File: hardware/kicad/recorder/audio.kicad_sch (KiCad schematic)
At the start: 20 parts, among them U2 ES8311, U6 NS4150B, Y1 12.288MHz

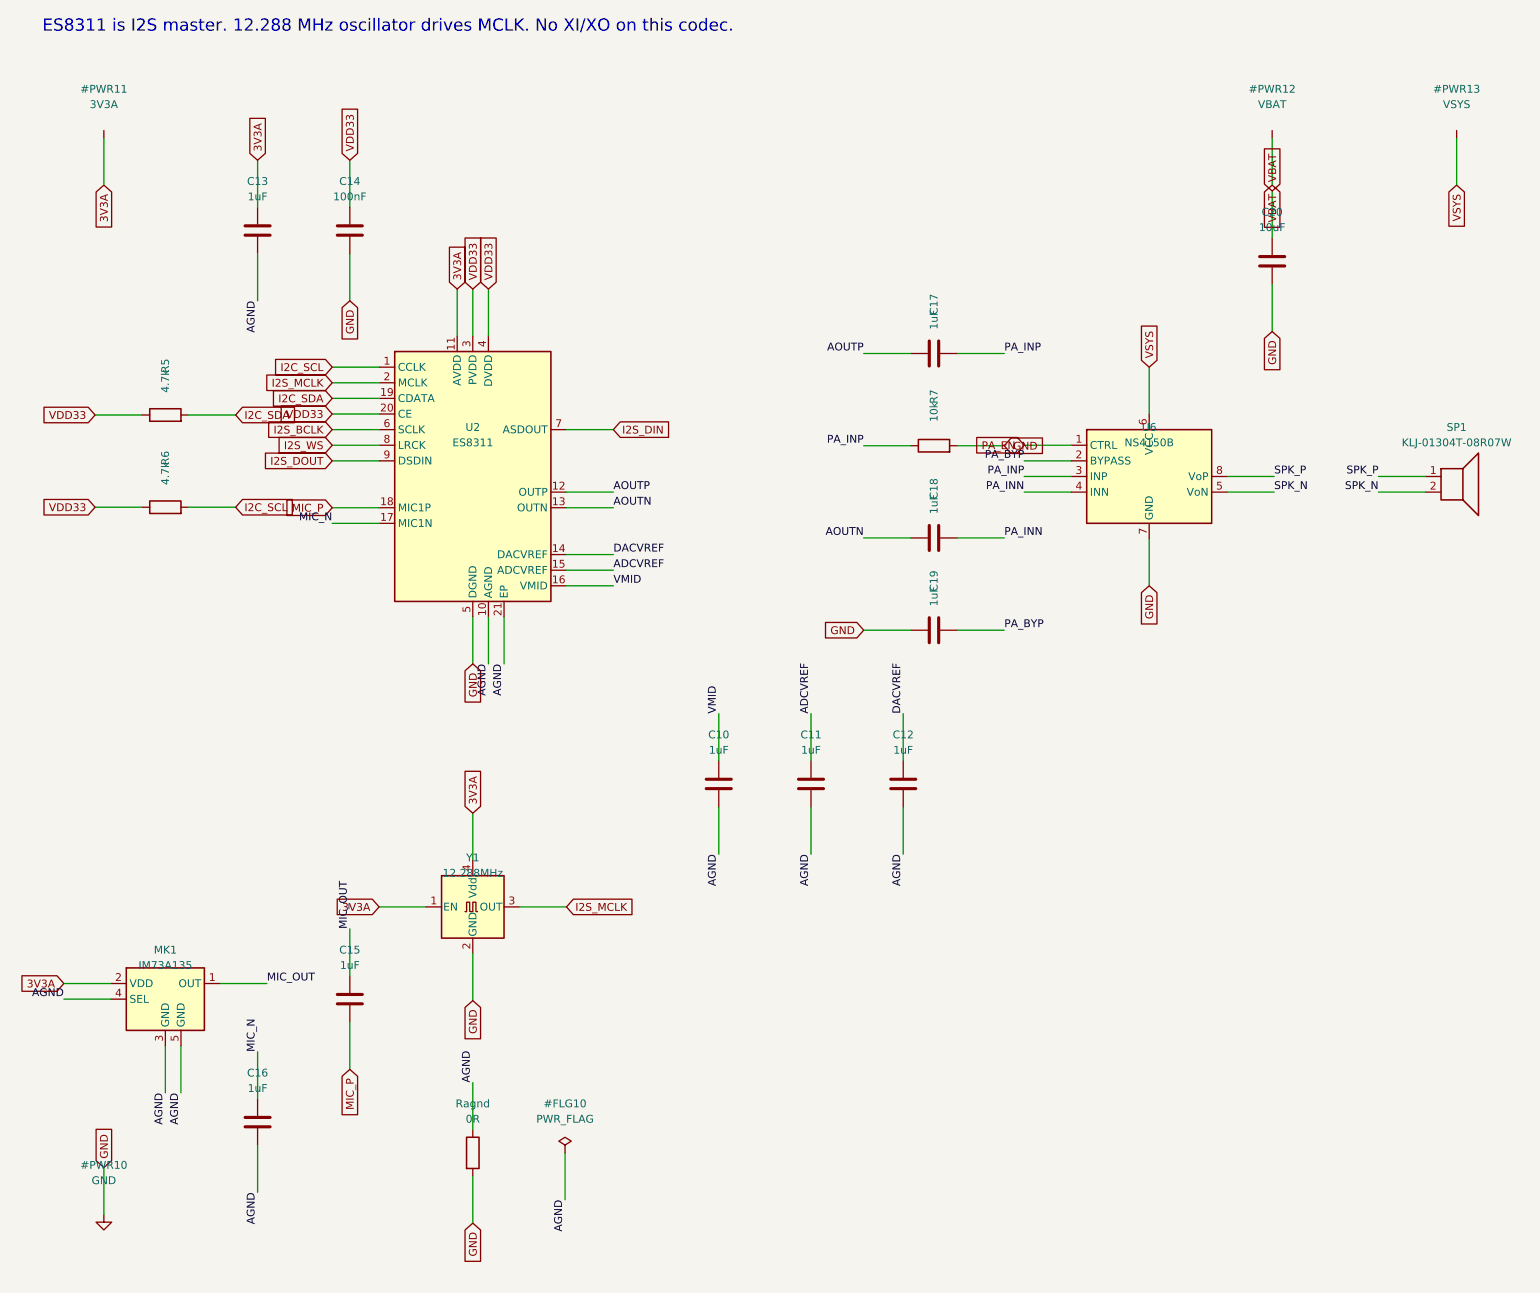
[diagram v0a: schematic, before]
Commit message: Keep J1 off SMT and fix MK1 pinout plus the 2.8 V analog rail.
J1 is a vertical 1x4 that will not fit under the lid, and the tails poke
toward the phone. Flag it exclude_from_bom so JLCPCB does not wave-solder
it. Keep C124378 in docs/bom.md and write jlcpcb_extra.csv so the header
can still be ordered as loose extra parts.

IM73A135 pin 3 is OUT-, a ~250 ohm amplifier output, not GND. Leave it
open; C15 still AC-couples OUT+ and C16 still takes codec MIC_N to AGND.
U8 is now LP5907-2.8 (C186700) because the capsule VDD abs max is 3.0 V.
ES8311 AVDD is 1.7-3.6 V and Y1 is 1.71-3.63 V, so the analog island can
sit at 2.8 V. Digital IO stays on VDD33.

Co-authored-by: zachrobertson19 <zachrobertson19@gmail.com>
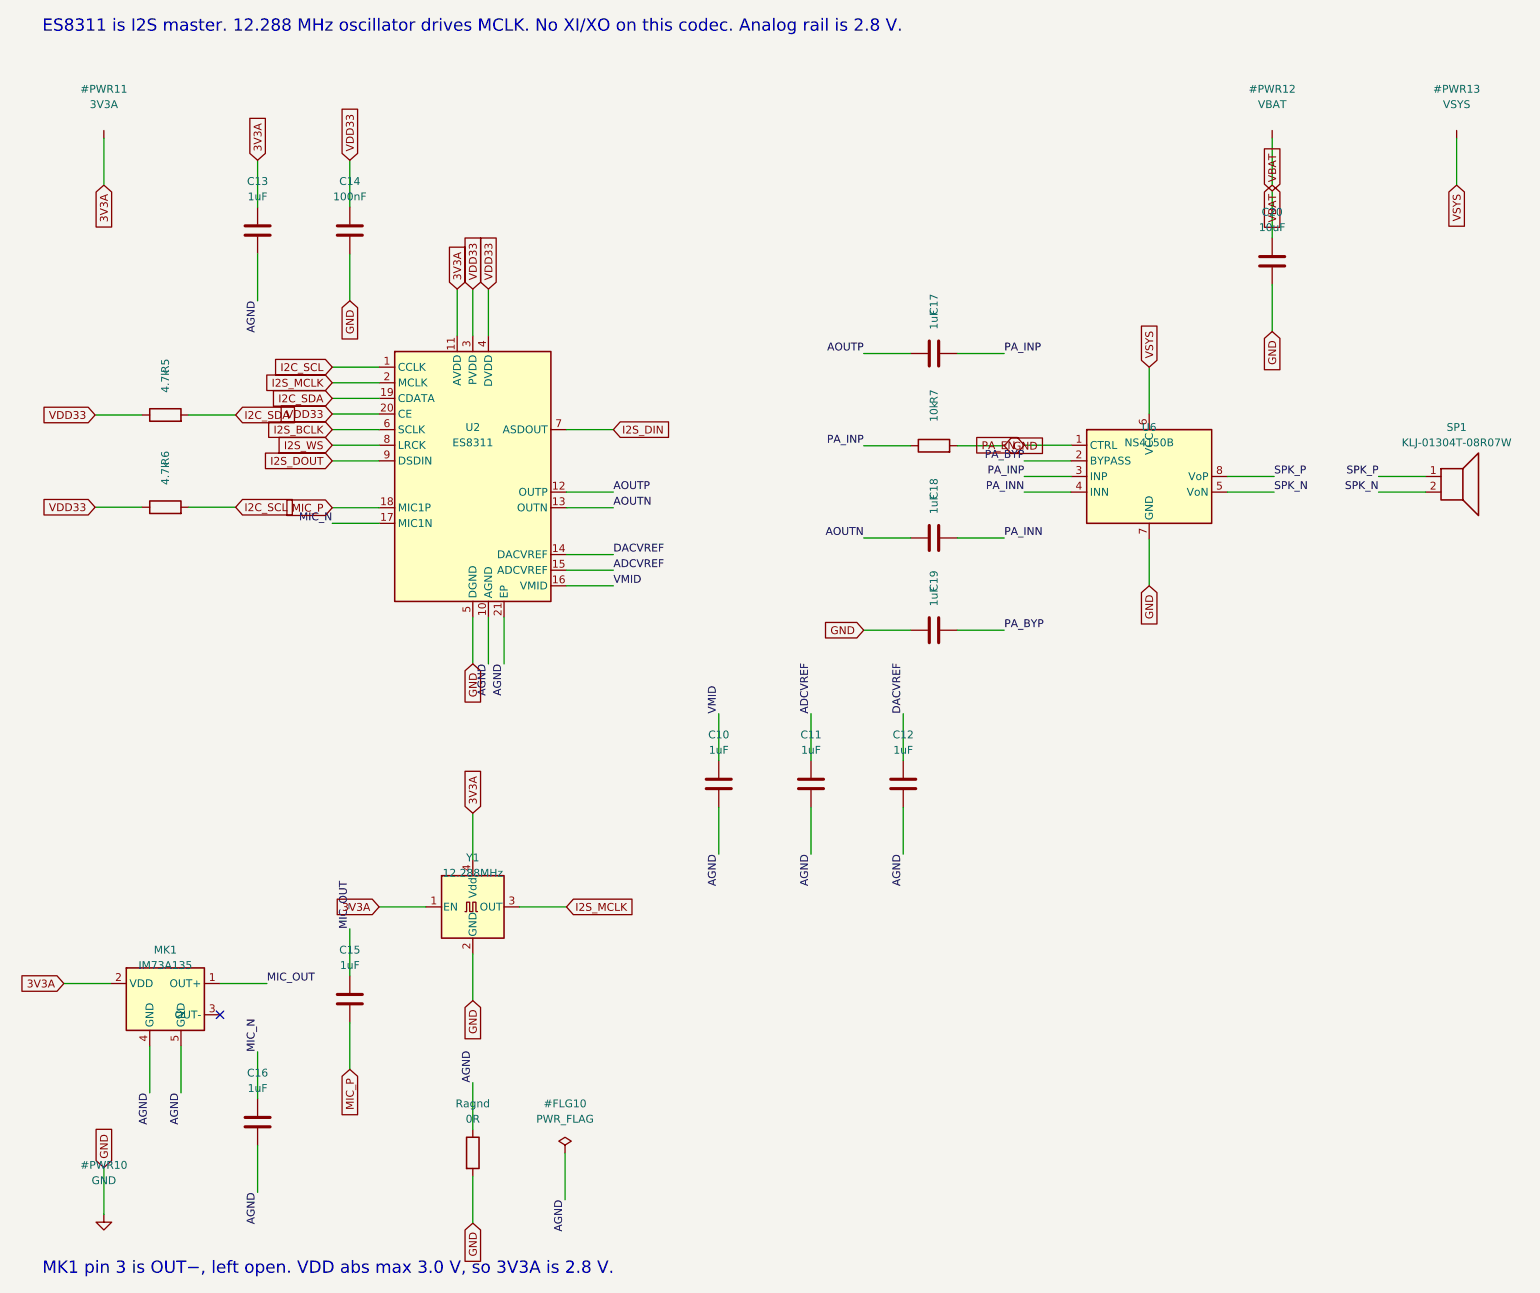
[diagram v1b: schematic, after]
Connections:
- net AGND: no longer MK1.3 (GND)
- no-connect marks 0 -> 1
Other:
- note added: "ES8311 is I2S master. 12.288 MHz oscillator drives MCLK. No XI/XO on this codec. Analog rail is 2.8 V."
- note added: "MK1 pin 3 is OUT−, left open. VDD abs max 3.0 V, so 3V3A is 2.8 V."
- note removed: "ES8311 is I2S master. 12.288 MHz oscillator drives MCLK. No XI/XO on this codec."
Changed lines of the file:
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@@
 		(rev "0")
 	)
-	(text "ES8311 is I2S master. 12.288 MHz oscillator drives MCLK. No XI/XO on this codec."
+	(text "ES8311 is I2S master. 12.288 MHz oscillator drives MCLK. No XI/XO on this codec. Analog rail is 2.8 V."
 		(exclude_from_sim no)
 		(at 20.00 18.00 0)
@@
 		(effects (font (size 1.27 1.27)) (justify right))
 	)
-	(wire
-		(pts (xy 40.00 182.62) (xy 40.00 190.24))
-		(stroke (width 0) (type default))
-	)
-	(label "AGND"
-		(at 40.00 190.24 270)
+	(no_connect
+		(at 48.89 177.54)
+	)
+	(wire
+		(pts (xy 37.46 182.62) (xy 37.46 190.24))
+		(stroke (width 0) (type default))
+	)
+	(label "AGND"
+		(at 37.46 190.24 270)
 		(effects (font (size 1.27 1.27)) (justify right bottom))
 	)
@@
 		(effects (font (size 1.27 1.27)) (justify right bottom))
 	)
-	(wire
-		(pts (xy 31.11 175.00) (xy 23.49 175.00))
-		(stroke (width 0) (type default))
-	)
-	(label "AGND"
-		(at 23.49 175.00 180)
-		(effects (font (size 1.27 1.27)) (justify right bottom))
-	)
-	(symbol
+	(text "MK1 pin 3 is OUT−, left open. VDD abs max 3.0 V, so 3V3A is 2.8 V."
+		(exclude_from_sim no)
+		(at 20.00 220.00 0)
+		(effects (font (size 2.0 2.0)) (justify left bottom))
+	)
+	(symbol
